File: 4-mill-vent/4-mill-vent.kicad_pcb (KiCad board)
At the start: 2 copper layers, 76.2 x 47.6 mm, 78 parts, among them J1 Fan, J2 Buzzer, J3 Power, J4 ICSP, Q1 MMBT3904, Q2 MMBT3904, Q3 PZT3904, Q4 PZT3904, Q5 TSM480P06CP, Q6 MMBT3904, Q7 MMBT3904, SW1 Power_off, SW2 Power_On, SW3 Fan_Down, SW4 Fan_Up, U1 LM321, U2 ATmega328P-AU, U3 TPSM84212EAB, U4 LM1117-5.0, Y1 16.000MHZ

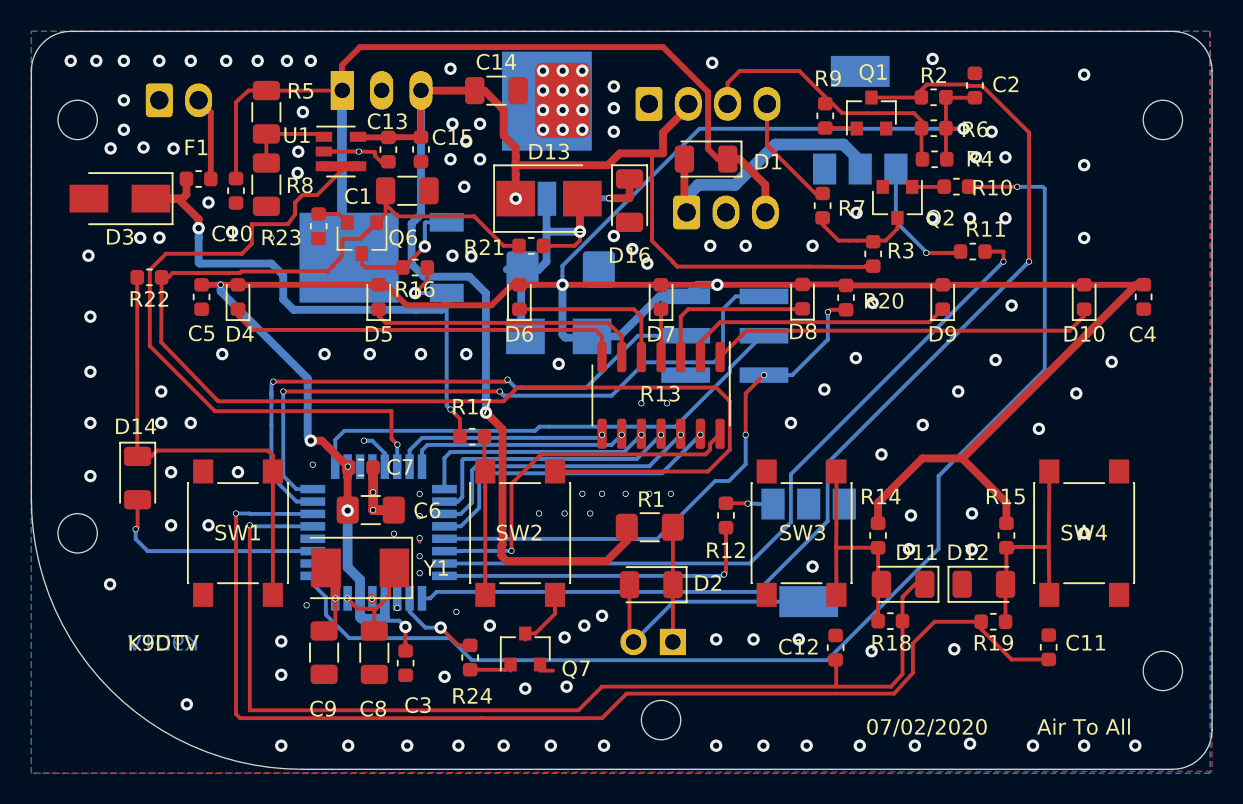
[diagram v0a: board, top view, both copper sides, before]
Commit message: BOM started
More updates to board
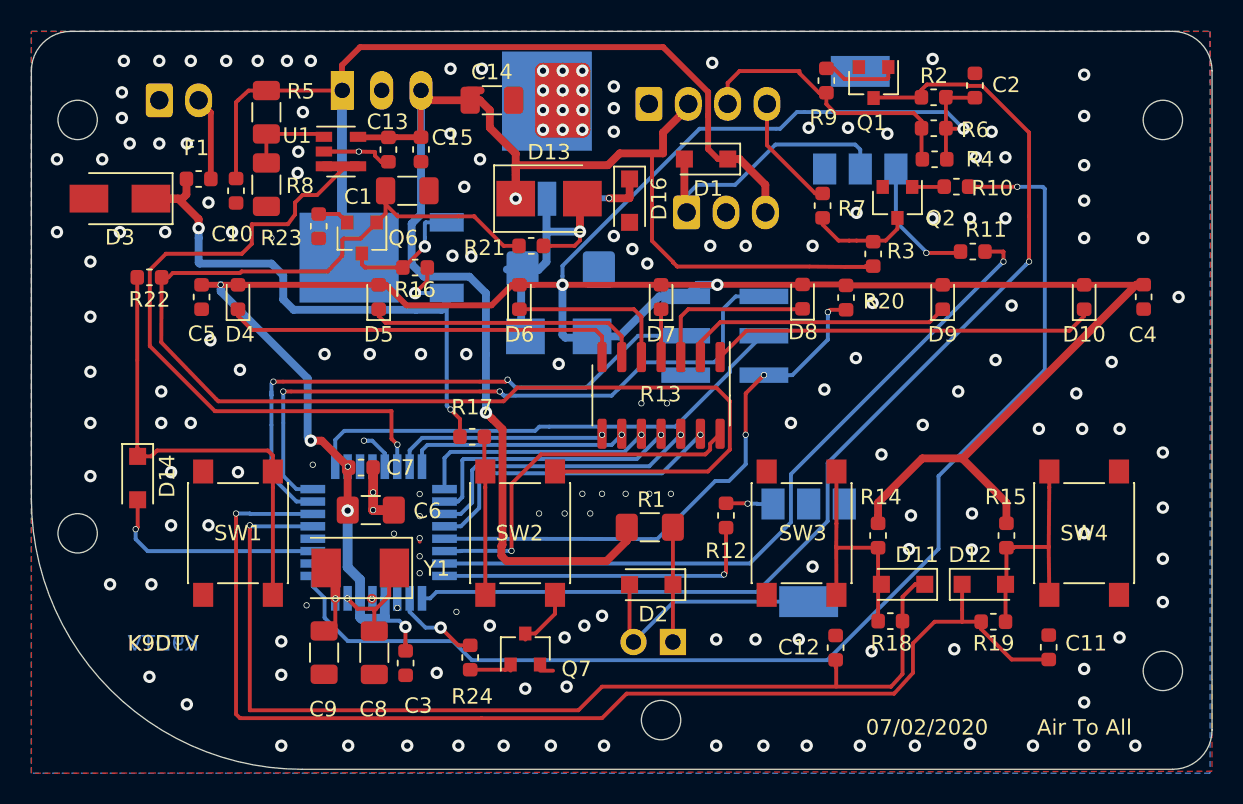
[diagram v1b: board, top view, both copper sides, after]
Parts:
- D1, D11, D12, D14, D16, D2: footprint Diode_SMD:D_1206_3216Metric -> Diode_SMD:D_SOD-123F
- D3: value 833-3SMAJ5936B-TP -> SMBJ5362B-TP
- moved R9 2.28 mm to (150.5, 71.5), turned to 90 degrees
- moved Q1 1.97 mm to (153.5, 71.6), turned to 270 degrees
- moved C14 0.69 mm to (128.9, 72.8)
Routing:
- net Net-(Q1-Pad1): track 2.06 -> 5.01 mm
- net +12V: track 107.2 -> 104.5 mm
- net Up: track 75.5 -> 77.9 mm
- net +5V: track 224.9 -> 225.8 mm
- net GND: vias 145 -> 163

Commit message: more updates
Found i added a extra resistor to raw_rpm, moved a few pins around the micro.. misc. clean up
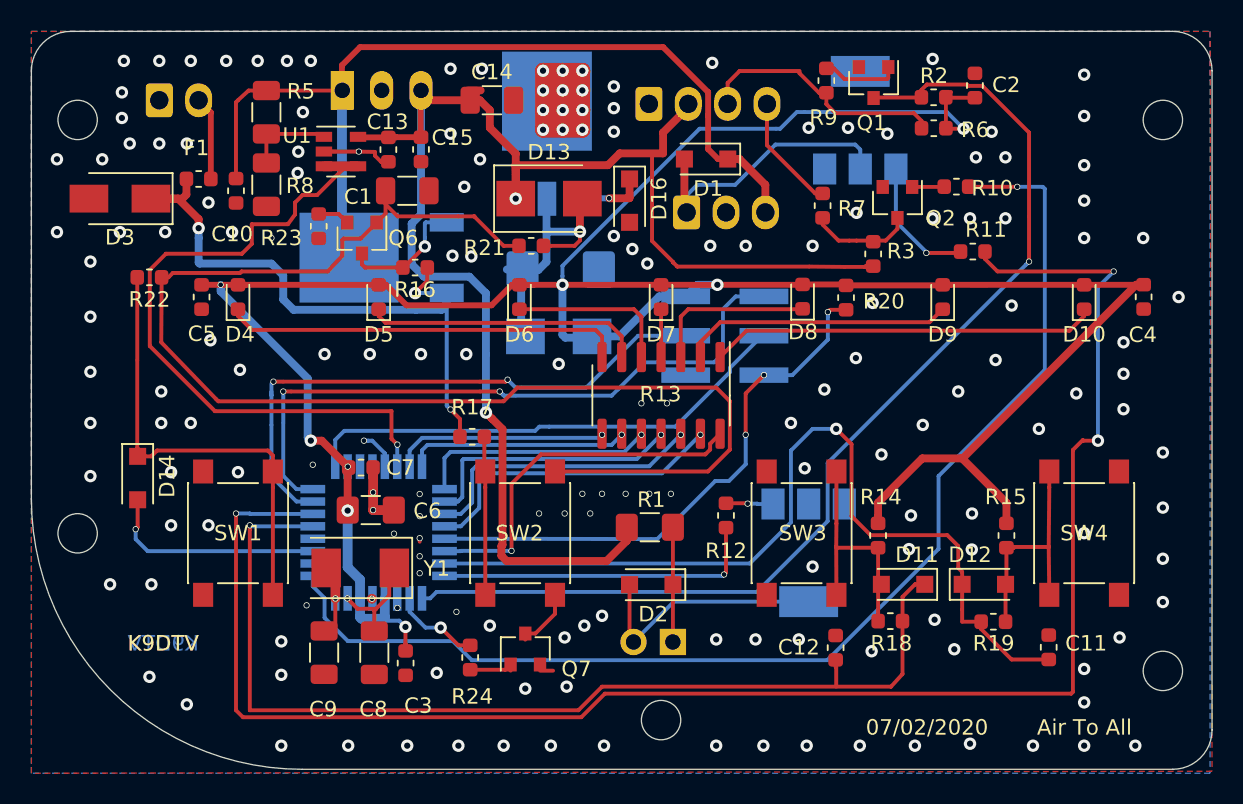
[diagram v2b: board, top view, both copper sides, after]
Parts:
- removed R4: 10k, Resistor_SMD:R_0603_1608Metric
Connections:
- U2 pad 14: Up -> Alarm
- U2 pad 31: Alarm -> Up
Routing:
- net Alarm: track 47.8 -> 110.5 mm, vias 1 -> 3
- net Up: track 77.9 -> 57.2 mm
- net +5V: track 225.8 -> 223.8 mm
- net Raw_RPM: track 18.5 -> 16.5 mm
- net GND: vias 163 -> 165

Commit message: Worked on moving parts around to improve ground plane
lots of parts and trace movement re-routing to make the ground plane lbetter.
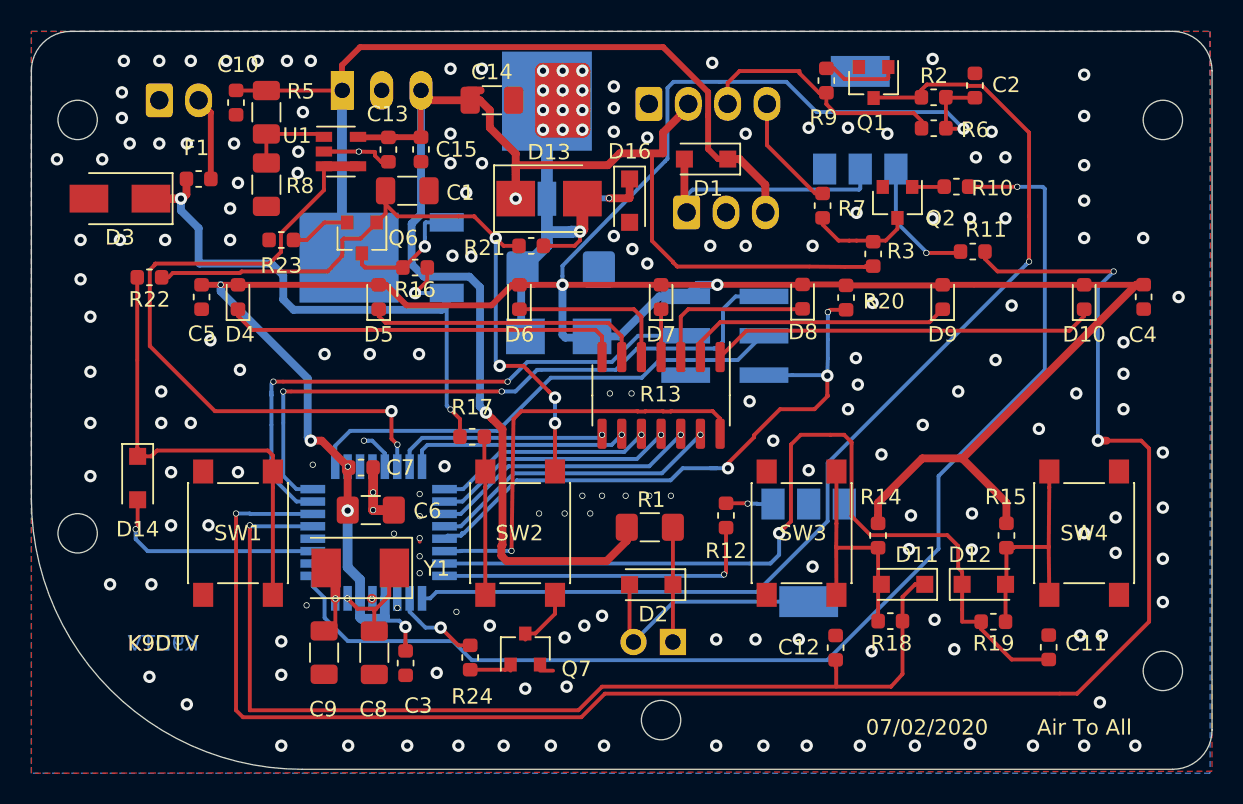
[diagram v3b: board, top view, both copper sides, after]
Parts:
- moved C10 5.69 mm to (112.4, 72.9)
- moved R23 2.57 mm to (115.3, 81.8), turned to 180 degrees
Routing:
- net Net-(C13-Pad1): track 90.8 -> 50.1 mm, vias 0 -> 4
- net Net-(C16-Pad1): track 50.6 -> 59.6 mm
- net SW_Batt: track 60.8 -> 55.6 mm
- net +5V: track 223.8 -> 228.1 mm
- net Reset: track 35.8 -> 40.0 mm
- net Alarm: track 110.5 -> 114.5 mm
- net LED7: track 23.7 -> 27.6 mm
- net Net-(Q6-Pad2): track 2.07 -> 3.94 mm
- net LED4: track 17.2 -> 15.8 mm
- net Buzzer-: track 18.9 -> 17.6 mm
- net LED6: track 20.2 -> 19.0 mm
- net LED5: track 18.6 -> 17.4 mm
- net LED3: track 15.3 -> 14.2 mm
- net Batt_V: track 45.7 -> 44.6 mm, vias 1 -> 2
- net Up: track 57.2 -> 57.9 mm
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
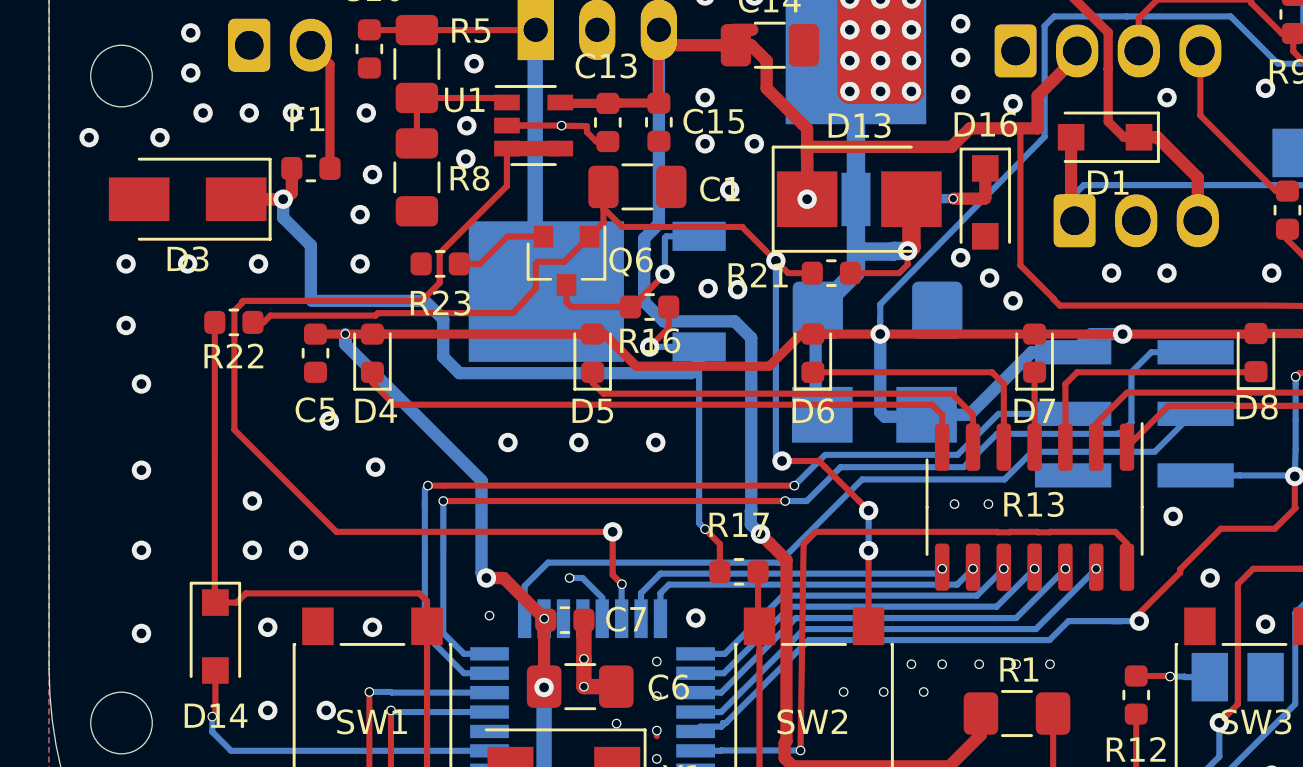
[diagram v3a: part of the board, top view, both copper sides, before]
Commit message: just making sure the lastest is pushed
going to be doing some testing today on power down and monitor. also going to change interface with fan, as there was no problems with the design on the test board.
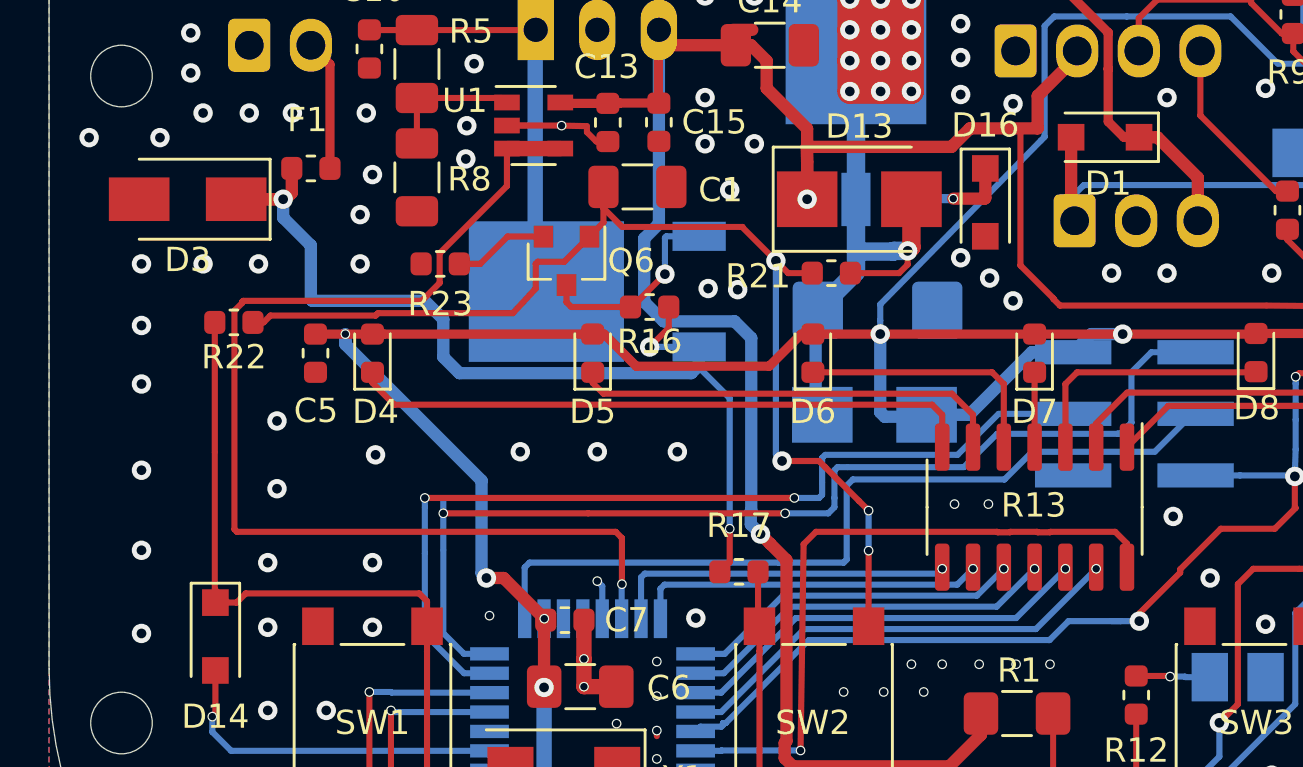
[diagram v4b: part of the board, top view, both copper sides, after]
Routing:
- net Batt_V: track 44.6 -> 47.1 mm, vias 2 -> 1
- net SCLK: track 32.0 -> 34.2 mm
- net MOSO: track 42.5 -> 43.6 mm
- net GND: track 13.1 -> 12.2 mm
- net MOSI: track 37.3 -> 37.9 mm

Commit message: last update for this round
last update for ver4 of board.
next will be ver5
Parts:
- removed Motor1: Mounting Holes, Connector_PinHeader_2.54mm:PinHeader_1x02_P2.54mm_Vertical
- removed Q1, Q2, Q7: MMBT3904, Package_TO_SOT_SMD:SOT-23
- removed R10: 1k, Resistor_SMD:R_0603_1608Metric
- removed R2, R3: 10k, Resistor_SMD:R_0603_1608Metric
- removed R24: 4.7k, Resistor_SMD:R_0603_1608Metric
- added H1: MountingHole_Pad, Connector_Molex:Molex_KK-254_AE-6410-02A_1x02_P2.54mm_Vertical, B.Cu at (140.6, 107.7)
- R1: footprint Resistor_SMD:R_1206_3216Metric_Pad1.42x1.75mm_HandSolder -> Resistor_SMD:R_0612_1632Metric_Pad1.18x3.40mm_HandSolder
- moved R9 12.3 mm to (162.8, 71.9), turned to 270 degrees
- moved R11 9.19 mm to (169.0, 81.2), turned to 270 degrees
- moved R7 6.75 mm to (151.9, 73.0), turned to 180 degrees
- moved R6 3.02 mm to (156.3, 71.8), turned to 270 degrees
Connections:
- R7 pad 1: Net-(Q2-Pad3) -> PWM
- R9 pad 2: Net-(Q1-Pad1) -> RPM
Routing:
- net +12V: track 104.3 -> 82.9 mm
- net Up: track 57.9 -> 46.9 mm
- net PWM: track 77.8 -> 88.6 mm
- net RPM: track 70.8 -> 61.3 mm
- net Net-(Q3-Pad1): track 8.47 -> 16.6 mm
- net Alarm: track 114.5 -> 106.5 mm
- net Net-(Q2-Pad3): track 6.71 -> 0.00 mm
- net Micro_power_Down: track 5.66 -> 0.00 mm, vias 1 -> 0
- net Net-(Q1-Pad1): track 5.01 -> 0.00 mm
- net Net-(D11-Pad2): track 15.7 -> 10.8 mm
- net Raw_RPM: track 16.5 -> 21.3 mm
- net Net-(C13-Pad1): track 50.1 -> 46.4 mm
- net +5V: track 228.1 -> 224.6 mm
- net PWM_Drive: track 7.55 -> 4.45 mm
- net Net-(Q7-Pad1): track 2.83 -> 0.00 mm
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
